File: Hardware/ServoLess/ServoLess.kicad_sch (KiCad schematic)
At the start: 82 parts, among them J1 XT30PW-M, J2 USB_C_Receptacle_USB2.0, J3 Conn_01x02_MountingPin, J6 Conn_01x04_MountingPin, SW1 SW_Push, SW2 SW_Push, U1 S8050, U2 S8050, U3 ESP32-S3FN8, U4 CH343P, U5 TPS54202DDC, U6 SPX3819M5-L-3-3, U7 AMS1117-3.3, U8 TJA1050T, Y1 40MHz 12pF 10ppm

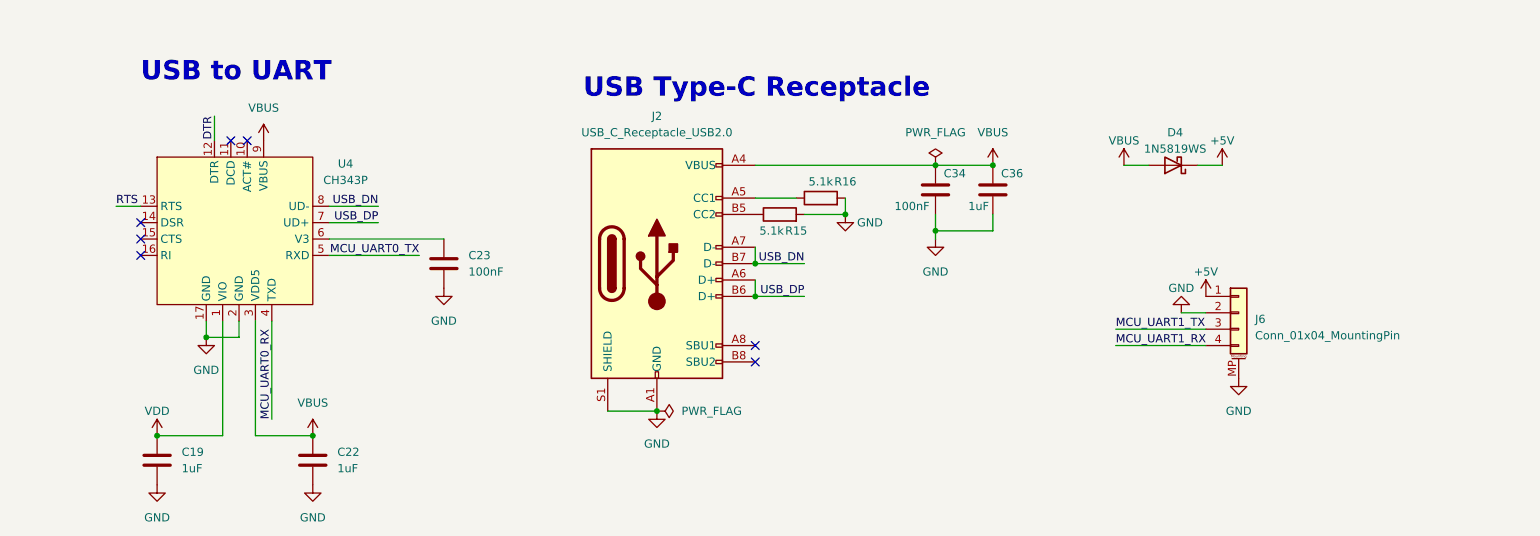
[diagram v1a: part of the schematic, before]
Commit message: add curr vel pos loops
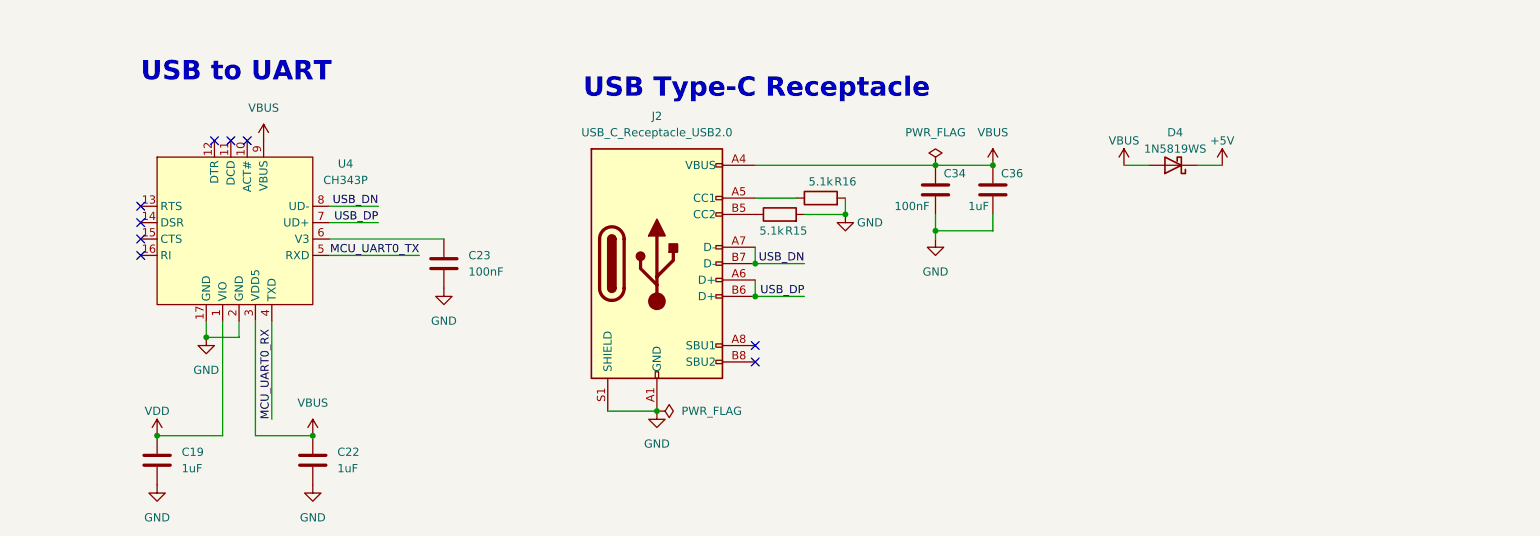
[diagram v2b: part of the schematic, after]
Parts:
- removed J6: Conn_01x04_MountingPin, Connector_JST:JST_SH_SM04B-SRSS-TB_1x04-1MP_P1.00mm_Horizontal, symbol Connector_Generic_MountingPin:Conn_01x04_MountingPin
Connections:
- net DTR: no longer U4.12 (DTR)
- net RTS: no longer U4.13 (RTS)
- no-connect marks 33 -> 35
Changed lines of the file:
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@@
   (no_connect (at 27.94 67.31))
   (no_connect (at 95.25 125.73))
+  (no_connect (at 191.77 203.2))
   (no_connect (at 161.29 85.09))
   (no_connect (at 95.25 90.17))
   (no_connect (at 161.29 146.05))
+  (no_connect (at 203.2 193.04))
   (no_connect (at 205.74 193.04))
   (no_connect (at 95.25 133.35))
@@
     (stroke (width 0) (type default))
   )
-  (wire (pts (xy 342.9 222.25) (xy 356.87 222.25))
-    (stroke (width 0) (type default))
-  )
   (wire (pts (xy 82.55 143.51) (xy 95.25 143.51))
     (stroke (width 0) (type default))
@@
     (stroke (width 0) (type default))
   )
-  (wire (pts (xy 342.9 224.79) (xy 356.87 224.79))
-    (stroke (width 0) (type default))
-  )
   (wire (pts (xy 95.25 95.25) (xy 86.36 95.25))
     (stroke (width 0) (type default))
@@
     (stroke (width 0) (type default))
   )
-  (wire (pts (xy 203.2 189.23) (xy 203.2 193.04))
-    (stroke (width 0) (type default))
-  )
   (wire (pts (xy 287.02 209.55) (xy 287.02 212.09))
     (stroke (width 0) (type default))
@@
     (stroke (width 0) (type default))
   )
-  (wire (pts (xy 187.96 203.2) (xy 191.77 203.2))
-    (stroke (width 0) (type default))
-  )
   (wire (pts (xy 196.85 48.26) (xy 204.47 48.26))
     (stroke (width 0) (type default))
@@
     (stroke (width 0) (type default))
   )
-  (wire (pts (xy 353.06 219.71) (xy 356.87 219.71))
-    (stroke (width 0) (type default))
-  )
   (wire (pts (xy 353.06 78.74) (xy 349.25 78.74))
     (stroke (width 0) (type default))
@@
     (effects (font (size 1.27 1.27)) (justify right bottom))
   )
-  (label "RTS" (at 187.96 203.2 0) (fields_autoplaced)
-    (effects (font (size 1.27 1.27)) (justify left bottom))
-  )
   (label "RTS" (at 34.29 215.9 0) (fields_autoplaced)
     (effects (font (size 1.27 1.27)) (justify left bottom))
@@
     (effects (font (size 1.27 1.27)) (justify right bottom))
   )
-  (label "MCU_UART1_RX" (at 342.9 224.79 0) (fields_autoplaced)
-    (effects (font (size 1.27 1.27)) (justify left bottom))
-  )
   (label "USB_DP" (at 294.64 217.17 180) (fields_autoplaced)
     (effects (font (size 1.27 1.27)) (justify right bottom))
@@
     (effects (font (size 1.27 1.27)) (justify right bottom))
   )
-  (label "DTR" (at 203.2 189.23 270) (fields_autoplaced)
-    (effects (font (size 1.27 1.27)) (justify right bottom))
-  )
-  (label "MCU_UART1_TX" (at 342.9 222.25 0) (fields_autoplaced)
-    (effects (font (size 1.27 1.27)) (justify left bottom))
-  )
   (label "MCU_EN" (at 68.58 193.04 180) (fields_autoplaced)
     (effects (font (size 1.27 1.27)) (justify right bottom))
@@
     )
   )
-  (symbol (lib_id "power:GND") (at 361.95 229.87 0) (unit 1)
-    (in_bom yes) (on_board yes) (dnp no) (fields_autoplaced)
-    (property "Reference" "#PWR013" (at 361.95 236.22 0)
-      (effects (font (size 1.27 1.27)) hide)
-    )
-    (property "Value" "GND" (at 361.95 234.95 0)
-      (effects (font (size 1.27 1.27)))
-    )
-    (property "Footprint" "" (at 361.95 229.87 0)
-      (effects (font (size 1.27 1.27)) hide)
-    )
-    (property "Datasheet" "" (at 361.95 229.87 0)
-      (effects (font (size 1.27 1.27)) hide)
-    )
-    (pin "1")
-    (instances
-      (project "ServoLess"
-        (path "/749e2666-eeca-46c2-af70-601d6adec38d"
-          (reference "#PWR013") (unit 1)
-        )
-      )
-    )
-  )
   (symbol (lib_id "power:GND") (at 128.27 151.13 0) (unit 1)
     (in_bom yes) (on_board yes) (dnp no) (fields_autoplaced)
@@
     )
   )
-  (symbol (lib_id "Connector_Generic_MountingPin:Conn_01x04_MountingPin") (at 361.95 219.71 0) (unit 1)
-    (in_bom yes) (on_board yes) (dnp no) (fields_autoplaced)
-    (property "Reference" "J6" (at 364.49 220.7006 0)
-      (effects (font (size 1.27 1.27)) (justify left))
-    )
-    (property "Value" "Conn_01x04_MountingPin" (at 364.49 223.2406 0)
-      (effects (font (size 1.27 1.27)) (justify left))
-    )
-    (property "Footprint" "Connector_JST:JST_SH_SM04B-SRSS-TB_1x04-1MP_P1.00mm_Horizontal" (at 361.95 219.71 0)
-      (effects (font (size 1.27 1.27)) hide)
-    )
-    (property "Datasheet" "~" (at 361.95 219.71 0)
-      (effects (font (size 1.27 1.27)) hide)
-    )
-    (pin "1")
-    (pin "2")
-    (pin "3")
-    (pin "4")
-    (pin "MP")
-    (instances
-      (project "ServoLess"
-        (path "/749e2666-eeca-46c2-af70-601d6adec38d"
-          (reference "J6") (unit 1)
-        )
-      )
-    )
-  )
   (symbol (lib_id "power:VDD") (at 194.31 238.76 0) (unit 1)
     (in_bom yes) (on_board yes) (dnp no) (fields_autoplaced)
@@
     )
   )
-  (symbol (lib_id "power:+5V") (at 356.87 217.17 0) (unit 1)
-    (in_bom yes) (on_board yes) (dnp no) (fields_autoplaced)
-    (property "Reference" "#PWR059" (at 356.87 220.98 0)
-      (effects (font (size 1.27 1.27)) hide)
-    )
-    (property "Value" "+5V" (at 356.87 213.36 0)
-      (effects (font (size 1.27 1.27)))
-    )
-    (property "Footprint" "" (at 356.87 217.17 0)
-      (effects (font (size 1.27 1.27)) hide)
-    )
-    (property "Datasheet" "" (at 356.87 217.17 0)
-      (effects (font (size 1.27 1.27)) hide)
-    )
-    (pin "1")
-    (instances
-      (project "ServoLess"
-        (path "/749e2666-eeca-46c2-af70-601d6adec38d"
-          (reference "#PWR059") (unit 1)
-        )
-      )
-    )
-  )
   (symbol (lib_id "Device:D_TVS") (at 181.61 44.45 90) (unit 1)
     (in_bom yes) (on_board yes) (dnp no) (fields_autoplaced)
@@
         )
       )
-    )
-  )
-  (symbol (lib_id "power:GND") (at 353.06 219.71 180) (unit 1)
-    (in_bom yes) (on_board yes) (dnp no) (fields_autoplaced)
-    (property "Reference" "#PWR058" (at 353.06 213.36 0)
-      (effects (font (size 1.27 1.27)) hide)
-    )
-    (property "Value" "GND" (at 353.06 215.9 0)
-      (effects (font (size 1.27 1.27)))
-    )
-    (property "Footprint" "" (at 353.06 219.71 0)
-      (effects (font (size 1.27 1.27)) hide)
-    )
-    (property "Datasheet" "" (at 353.06 219.71 0)
-      (effects (font (size 1.27 1.27)) hide)
-    )
-    (pin "1")
-    (instances
-      (project "ServoLess"
-        (path "/749e2666-eeca-46c2-af70-601d6adec38d"
-          (reference "#PWR058") (unit 1)
-        )
-      )
